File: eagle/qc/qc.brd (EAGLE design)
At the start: 70.1 x 74.6 mm, 40 parts, among them IC1 IRFS7530, IC2 IRFS7530, IC3 IRFS7530, IC4 IRFS7530, IC5 IRFS7530, IC6 IRFS7530, U1 DRV8302

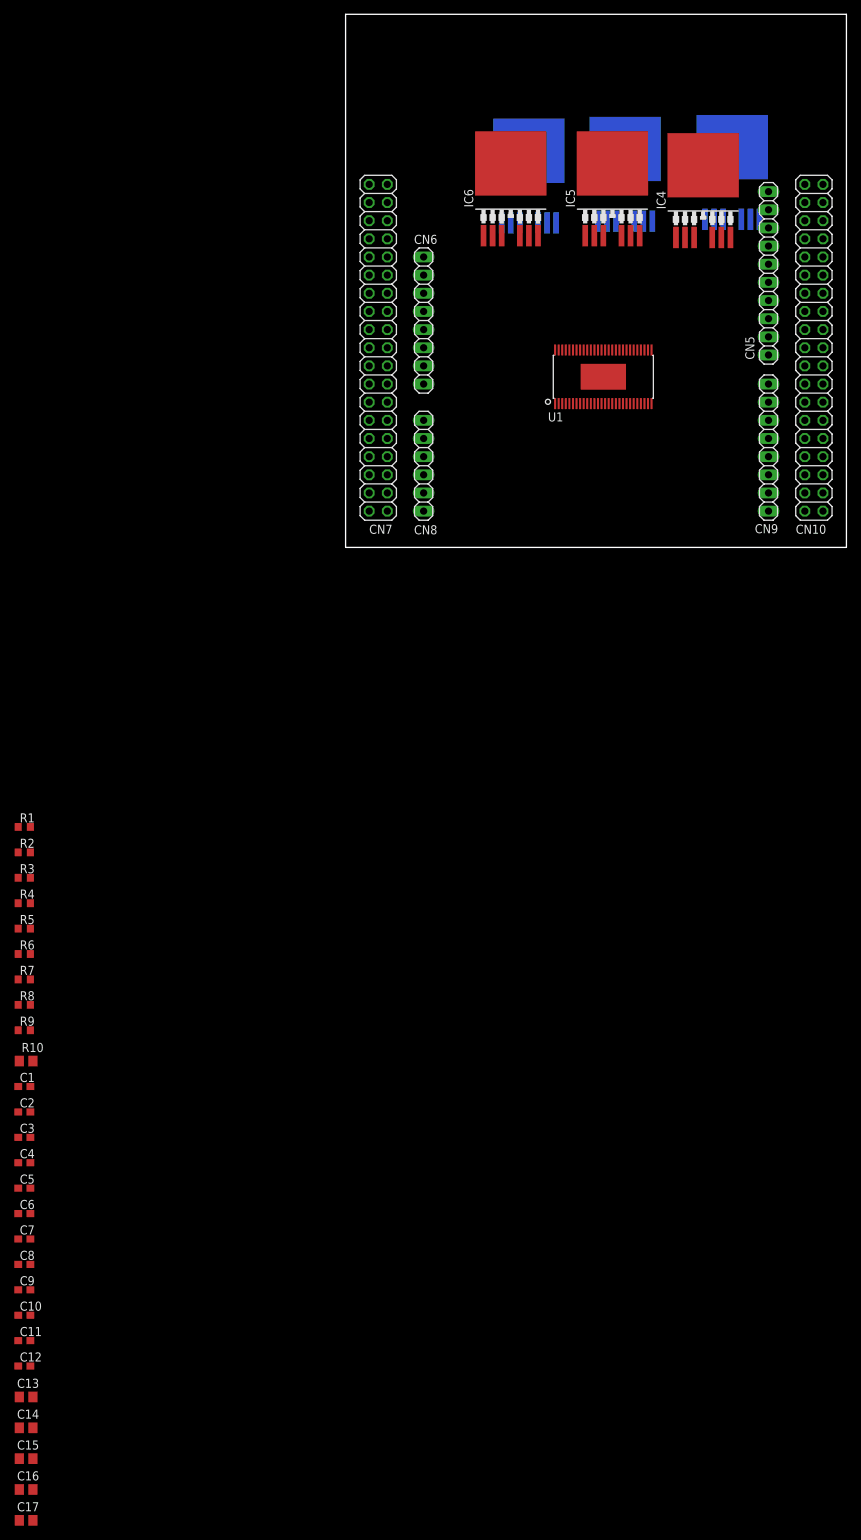
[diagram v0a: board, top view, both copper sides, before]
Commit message: added FETs and related circuitry for the motor drive, current sense
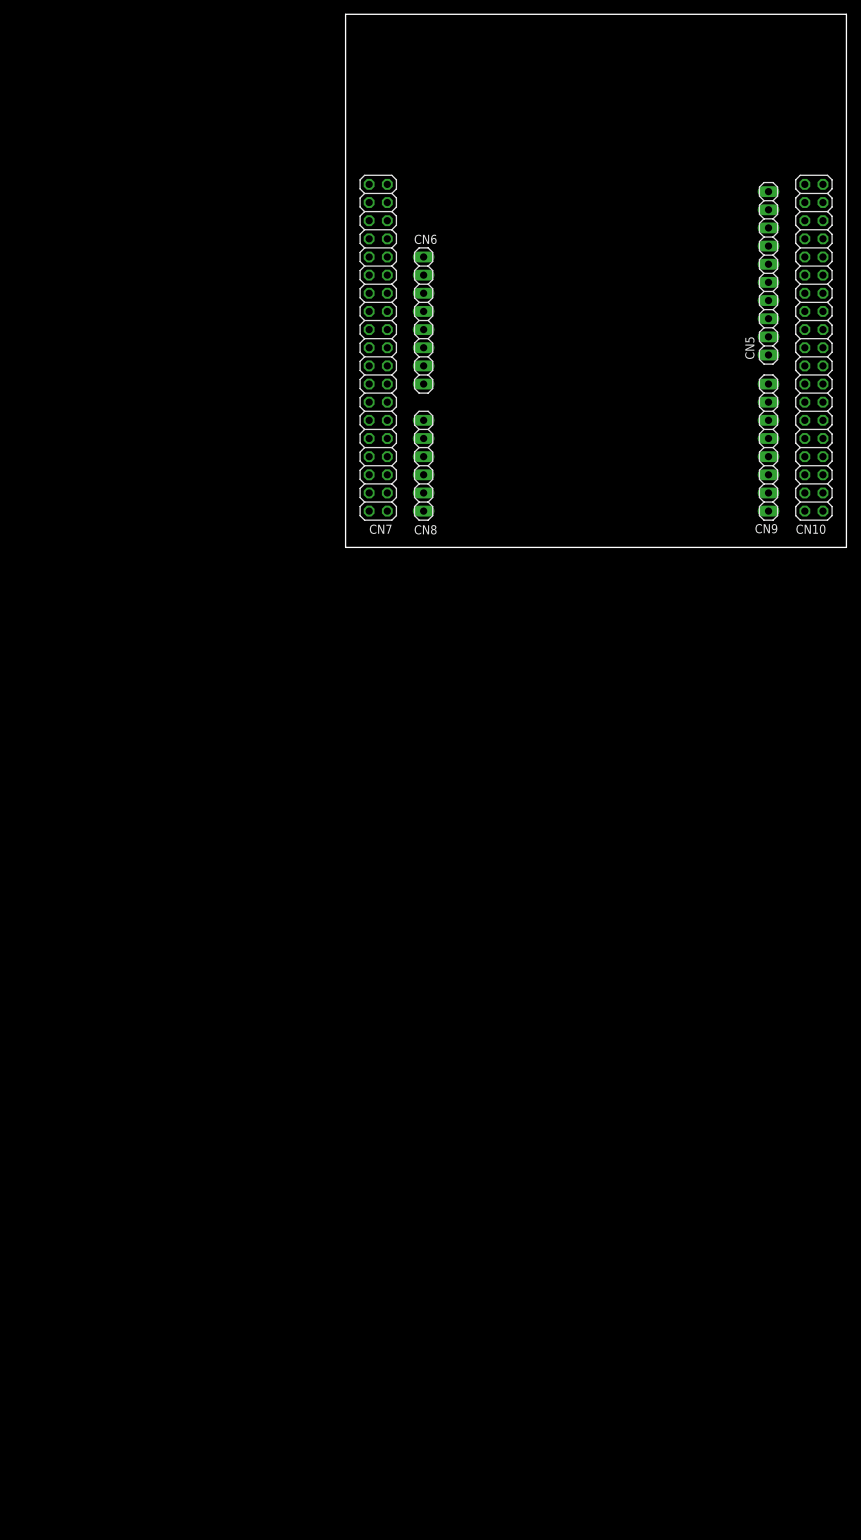
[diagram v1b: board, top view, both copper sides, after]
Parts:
- removed C1, C10, C11, C12, C2, C3, C4, C5, C6, C7, C8, C9: (no value), resistor:C0603
- removed C13, C14, C15, C16, C17: (no value), resistor:C0805
- removed IC1, IC2, IC3, IC4, IC5, IC6: IRFS7530, IRFS7530:PG-TO263-7-3
- removed R1, R2, R3, R4, R5, R6, R7, R8, R9: (no value), resistor:R0603
- removed R10: (no value), resistor:R0805
- removed U1: DRV8302, drv8302:DRV8302
